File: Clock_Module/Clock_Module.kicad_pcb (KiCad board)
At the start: 2 copper layers, 160 x 100 mm, 4 parts

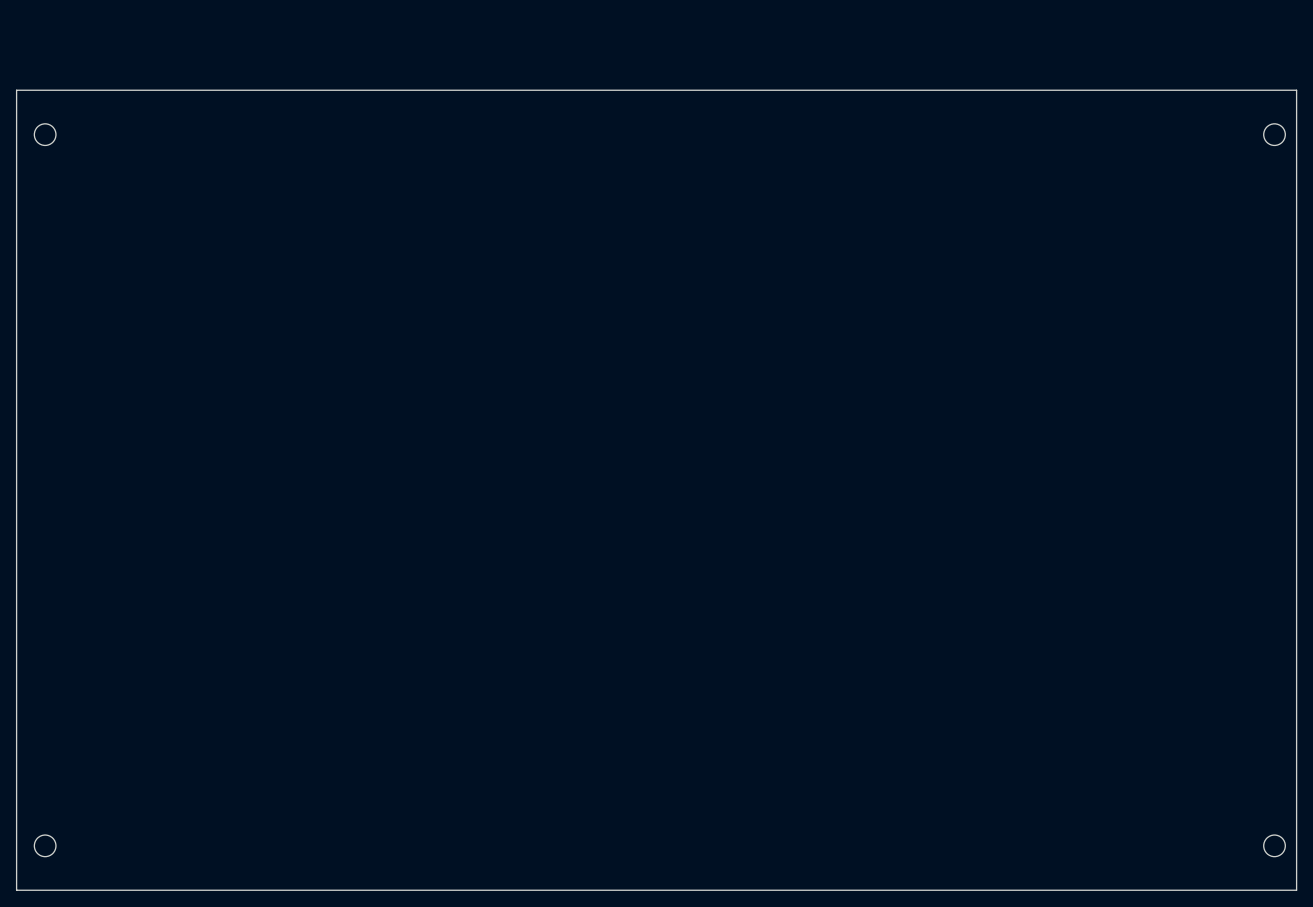
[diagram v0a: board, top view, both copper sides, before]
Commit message: Updated Schematic to PC104 standards, updated Simulation for intel-quartus, updated PCB constraints, and edited board layout
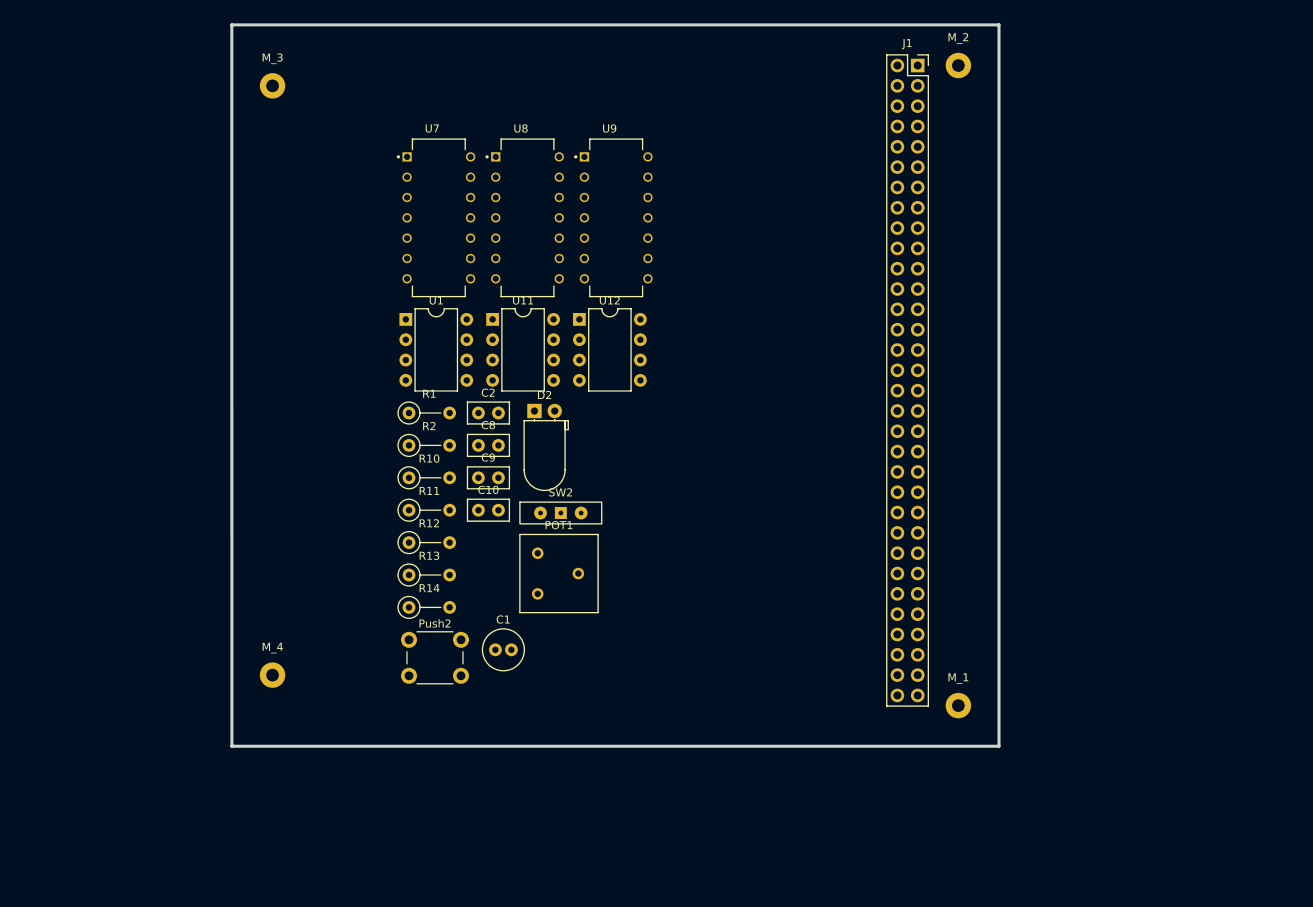
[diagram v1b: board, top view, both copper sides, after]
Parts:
- removed MH1, MH2, MH3, MH4: MountingHole_2.7mm_M2.5_DIN965, MountingHole:MountingHole_2.7mm_M2.5_DIN965
- added C1: 1µF, Capacitor_THT:C_Radial_D5.0mm_H11.0mm_P2.00mm, F.Cu at (114.8, 114.9)
- added C10: .01µF, Capacitor_THT:C_Disc_D5.0mm_W2.5mm_P2.50mm, F.Cu at (112.7, 97.5)
- added C2: .01µF, Capacitor_THT:C_Disc_D5.0mm_W2.5mm_P2.50mm, F.Cu at (112.7, 85.3)
- added C8: .01µF, Capacitor_THT:C_Disc_D5.0mm_W2.5mm_P2.50mm, F.Cu at (112.7, 89.4)
- added C9: .01µF, Capacitor_THT:C_Disc_D5.0mm_W2.5mm_P2.50mm, F.Cu at (112.7, 93.4)
- added D2: LED, LED_THT:LED_D5.0mm_Horizontal_O1.27mm_Z3.0mm, F.Cu at (119.7, 85.1)
- added J1: PC104, Connector_PinSocket_2.54mm:PinSocket_2x32_P2.54mm_Vertical, F.Cu at (167.6, 41.9)
- added M_1: MountingHole_2.5mm_Pad, MountingHole:MountingHole_2.5mm_Pad, F.Cu at (172.7, 121.9)
- added M_2: MountingHole_2.5mm_Pad, MountingHole:MountingHole_2.5mm_Pad, F.Cu at (172.7, 41.9)
- added M_3: MountingHole_2.5mm_Pad, MountingHole:MountingHole_2.5mm_Pad, F.Cu at (87.0, 44.5)
- added M_4: MountingHole_2.5mm_Pad, MountingHole:MountingHole_2.5mm_Pad, F.Cu at (87.0, 118.1)
- added POT1: 1M, Potentiometer_THT:Potentiometer_Bourns_3386F_Vertical, F.Cu at (120.1, 108.0)
- added Push2: SW_Push, Button_Switch_THT:SW_PUSH_6mm_H4.3mm, F.Cu at (104.0, 113.7)
- added R1: 1K, Resistor_THT:R_Axial_DIN0207_L6.3mm_D2.5mm_P5.08mm_Vertical, F.Cu at (104.0, 85.3)
- added R10: 1K, Resistor_THT:R_Axial_DIN0207_L6.3mm_D2.5mm_P5.08mm_Vertical, F.Cu at (104.0, 93.4)
- added R11: 1K, Resistor_THT:R_Axial_DIN0207_L6.3mm_D2.5mm_P5.08mm_Vertical, F.Cu at (104.0, 97.5)
- added R12: 1K, Resistor_THT:R_Axial_DIN0207_L6.3mm_D2.5mm_P5.08mm_Vertical, F.Cu at (104.0, 101.5)
- added R13: 1M, Resistor_THT:R_Axial_DIN0207_L6.3mm_D2.5mm_P5.08mm_Vertical, F.Cu at (104.0, 105.6)
- added R14: 1K, Resistor_THT:R_Axial_DIN0207_L6.3mm_D2.5mm_P5.08mm_Vertical, F.Cu at (104.0, 109.6)
- added R2: 1K, Resistor_THT:R_Axial_DIN0207_L6.3mm_D2.5mm_P5.08mm_Vertical, F.Cu at (104.0, 89.4)
- added SW2: SW_Wuerth_450301014042, MyFootPrints:SW_Slide-Jameco-SS-12E17-G020, F.Cu at (123.0, 97.8)
- added U1: LM555xN, Package_DIP:DIP-8_W7.62mm, F.Cu at (103.7, 73.6)
- added U11: LM555xN, Package_DIP:DIP-8_W7.62mm, F.Cu at (114.5, 73.6)
- added U12: LM555xN, Package_DIP:DIP-8_W7.62mm, F.Cu at (125.3, 73.6)
- added U7: 74LS08, MyFootPrints:SN74LS08N, F.Cu at (107.8, 61.0)
- added U8: 74LS32, MyFootPrints:SN74LS32N, F.Cu at (118.9, 61.0)
- added U9: 74LS04, MyFootPrints:SN74LS04N, F.Cu at (129.9, 61.0)
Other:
- board size 160 x 100 mm -> 95.9 x 90.2 mm
- board text removed: "Mounting holes are optional Keepout areas are for for guide rails"

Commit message: partially complete pcb and updated schematic with bypass capacitors
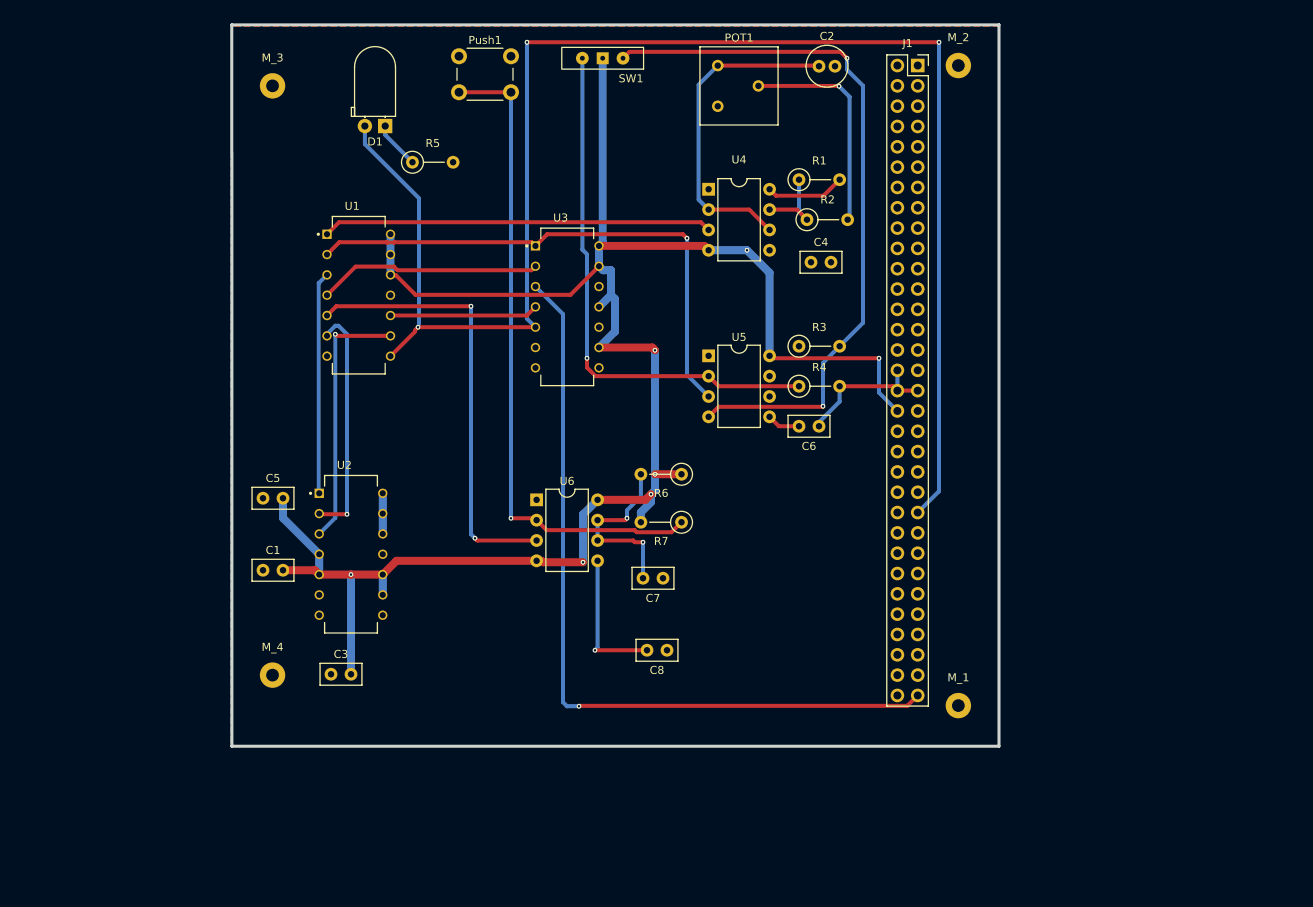
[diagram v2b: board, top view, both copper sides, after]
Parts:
- removed C10, C9: .01µF, Capacitor_THT:C_Disc_D5.0mm_W2.5mm_P2.50mm
- removed D2: LED, LED_THT:LED_D5.0mm_Horizontal_O1.27mm_Z3.0mm
- removed Push2: SW_Push, Button_Switch_THT:SW_PUSH_6mm_H4.3mm
- removed R10, R11, R12, R14: 1K, Resistor_THT:R_Axial_DIN0207_L6.3mm_D2.5mm_P5.08mm_Vertical
- removed R13: 1M, Resistor_THT:R_Axial_DIN0207_L6.3mm_D2.5mm_P5.08mm_Vertical
- removed SW2: SW_Wuerth_450301014042, MyFootPrints:SW_Slide-Jameco-SS-12E17-G020
- removed U11, U12: LM555xN, Package_DIP:DIP-8_W7.62mm
- removed U7: 74LS08, MyFootPrints:SN74LS08N
- removed U8: 74LS32, MyFootPrints:SN74LS32N
- removed U9: 74LS04, MyFootPrints:SN74LS04N
- added C3: .01µF, Capacitor_THT:C_Disc_D5.0mm_W2.5mm_P2.50mm, F.Cu at (94.3, 118.0)
- added C4: .01µF, Capacitor_THT:C_Disc_D5.0mm_W2.5mm_P2.50mm, F.Cu at (154.3, 66.5)
- added C5: .01µF, Capacitor_THT:C_Disc_D5.0mm_W2.5mm_P2.50mm, F.Cu at (85.8, 96.0)
- added C6: .01µF, Capacitor_THT:C_Disc_D5.0mm_W2.5mm_P2.50mm, F.Cu at (155.3, 87.0)
- added C7: .01µF, Capacitor_THT:C_Disc_D5.0mm_W2.5mm_P2.50mm, F.Cu at (135.8, 106.0)
- added D1: LED, LED_THT:LED_D5.0mm_Horizontal_O1.27mm_Z3.0mm, F.Cu at (101.1, 49.5)
- added Push1: SW_Push, Button_Switch_THT:SW_PUSH_6mm_H4.3mm, F.Cu at (110.3, 40.8)
- added R3: 1K, Resistor_THT:R_Axial_DIN0207_L6.3mm_D2.5mm_P5.08mm_Vertical, F.Cu at (152.8, 77.0)
- added R4: 1K, Resistor_THT:R_Axial_DIN0207_L6.3mm_D2.5mm_P5.08mm_Vertical, F.Cu at (152.8, 82.0)
- added R5: 1K, Resistor_THT:R_Axial_DIN0207_L6.3mm_D2.5mm_P5.08mm_Vertical, F.Cu at (104.5, 54.0)
- added R6: 1M, Resistor_THT:R_Axial_DIN0207_L6.3mm_D2.5mm_P5.08mm_Vertical, F.Cu at (138.1, 93.0)
- added R7: 1K, Resistor_THT:R_Axial_DIN0207_L6.3mm_D2.5mm_P5.08mm_Vertical, F.Cu at (138.1, 99.0)
- added SW1: Switch, MyFootPrints:SW_Slide-Jameco-SS-12E17-G020, F.Cu at (128.3, 41.0)
- added U2: 74LS32, MyFootPrints:SN74LS32N, F.Cu at (96.8, 103.0)
- added U3: 74LS04, MyFootPrints:SN74LS04N, F.Cu at (123.8, 72.1)
- added U4: LM555xN, Package_DIP:DIP-8_W7.62mm, F.Cu at (141.5, 57.4)
- added U5: LM555xN, Package_DIP:DIP-8_W7.62mm, F.Cu at (141.5, 78.2)
- added U6: LM555xN, Package_DIP:DIP-8_W7.62mm, F.Cu at (120.0, 96.2)
- C1: value 1µF -> .01µF; footprint Capacitor_THT:C_Radial_D5.0mm_H11.0mm_P2.00mm -> Capacitor_THT:C_Disc_D5.0mm_W2.5mm_P2.50mm
- C2: value .01µF -> 1µF; footprint Capacitor_THT:C_Disc_D5.0mm_W2.5mm_P2.50mm -> Capacitor_THT:C_Radial_D5.0mm_H11.0mm_P2.00mm
- U1: value LM555xN -> 74LS08; footprint Package_DIP:DIP-8_W7.62mm -> MyFootPrints:SN74LS08N
- moved POT1 65.0 mm to (142.6, 47.0)
- moved C2 60.8 mm to (155.3, 42.0)
- moved R2 57.2 mm to (153.8, 61.2)
- moved R1 56.8 mm to (152.8, 56.2)
- moved C8 34.8 mm to (136.3, 115.0), turned to 180 degrees
- moved C1 30.7 mm to (85.8, 105.0)
- moved U1 6.61 mm to (97.8, 70.6)
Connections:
- C1 pad 1: Net-(U1-THR) -> GND
- C1 pad 2: GND -> 5V
- C2 pad 1: GND -> Net-(U4-THR)
- POT1 pad 3: Net-(U1-THR) -> Net-(U4-THR)
- R1 pad 1: Net-(U1-DIS) -> Net-(U4-DIS)
- R2 pad 1: Net-(U1-DIS) -> Net-(U4-DIS)
- U1 pad 1: GND -> /astable_out
- U1 pad 2: Net-(U1-THR) -> /bistable_out
- U1 pad 3: /astable_out -> Net-(U1-Pad3)
- U1 pad 4: 5V -> Net-(U1-Pad4)
- U1 pad 5: GND -> /monostable_out
- U1 pad 6: Net-(U1-THR) -> Net-(U1-Pad6)
- U1 pad 7: Net-(U1-DIS) -> GND
- U1 pad 8: 5V -> /CLK
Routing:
- net 5V: track 0.00 -> 256.9 mm, vias 0 -> 7
- net /CLK: track 0.00 -> 195.2 mm, vias 0 -> 3
- net /halt: track 0.00 -> 98.5 mm, vias 0 -> 1
- net Net-(SW1-C): track 0.00 -> 89.9 mm, vias 0 -> 2
- net Net-(U6-TR): track 0.00 -> 82.3 mm, vias 0 -> 1
- net /bistable_out: track 0.00 -> 67.6 mm, vias 0 -> 1
- net Net-(SW1-A): track 0.00 -> 66.4 mm, vias 0 -> 1
- net /monostable_out: track 0.00 -> 55.5 mm, vias 0 -> 2
- net /astable_out: track 0.00 -> 48.7 mm
- net Net-(U4-THR): track 0.00 -> 40.9 mm
- net Net-(U1-Pad9): track 0.00 -> 32.8 mm, vias 0 -> 1
- net Net-(U1-Pad6): track 0.00 -> 29.6 mm, vias 0 -> 1
- net Net-(U1-Pad4): track 0.00 -> 27.9 mm
- net Net-(U1-Pad3): track 0.00 -> 27.8 mm
- net Net-(POT1-Pad2): track 0.00 -> 27.4 mm, vias 0 -> 1
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- added copper zone on B.Cu, net GND
- added copper zone on F.Cu, net GND

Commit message: Routed PCB
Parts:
- added ?: , PCB_Art:GrayFox.F.Cu, F.Cu at (150.3, 107.0)
- added ?: , PCB_Art:GrayFox.F.SilkS, F.Cu at (150.3, 107.0)
- added ?: , PCB_Art:GrayFox.F.Mask, F.Cu at (150.3, 107.0)
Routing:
- net /CLK: track 195.2 -> 118.1 mm, vias 3 -> 4
- net 5V: track 256.9 -> 310.9 mm
- net /astable_out: track 48.7 -> 50.4 mm
- net Net-(U1-Pad6): track 29.6 -> 31.2 mm
- net Net-(U1-Pad9): track 32.8 -> 31.9 mm
- net GND: track 18.6 -> 19.1 mm

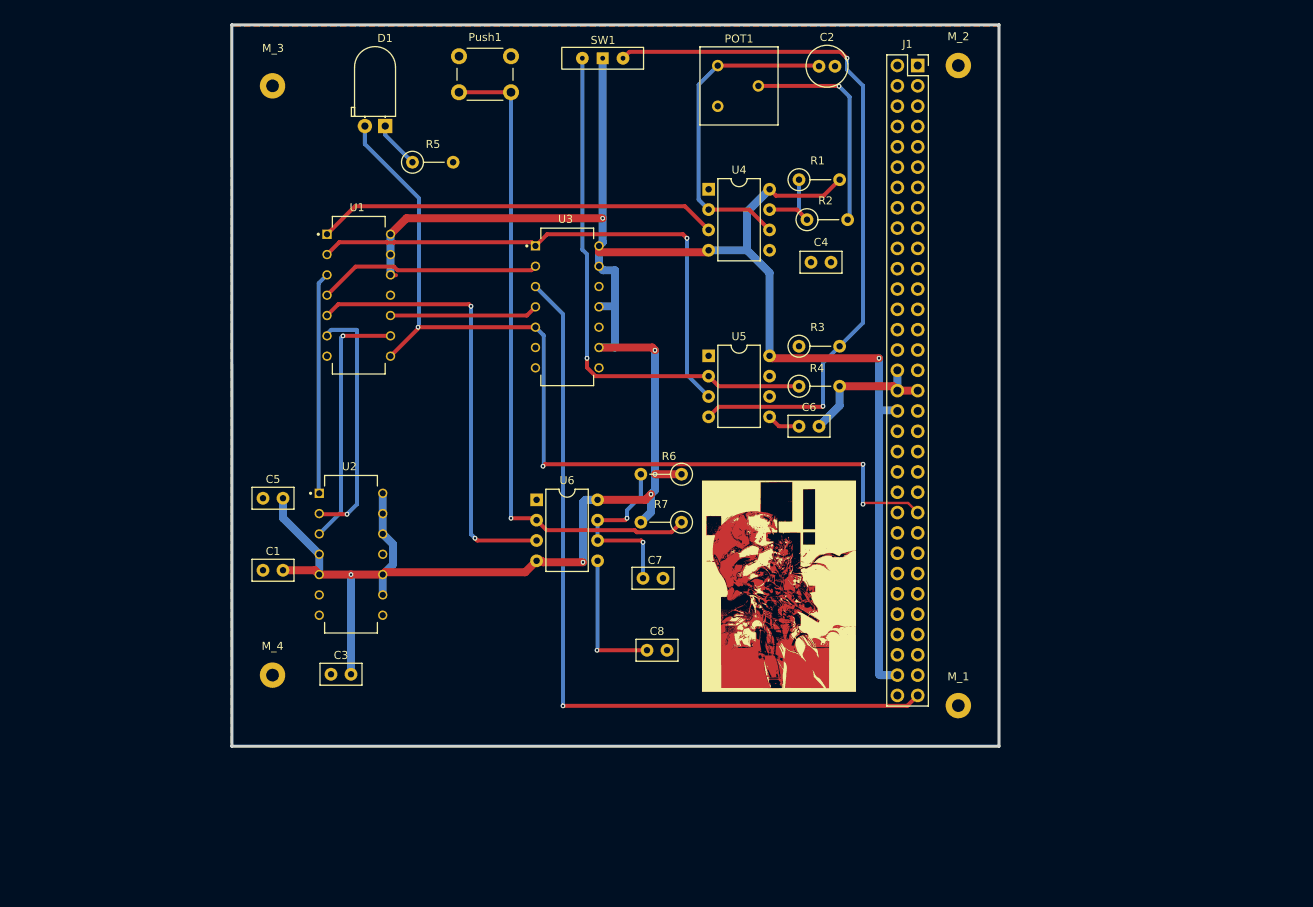
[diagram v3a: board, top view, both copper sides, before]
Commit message: completed clock module
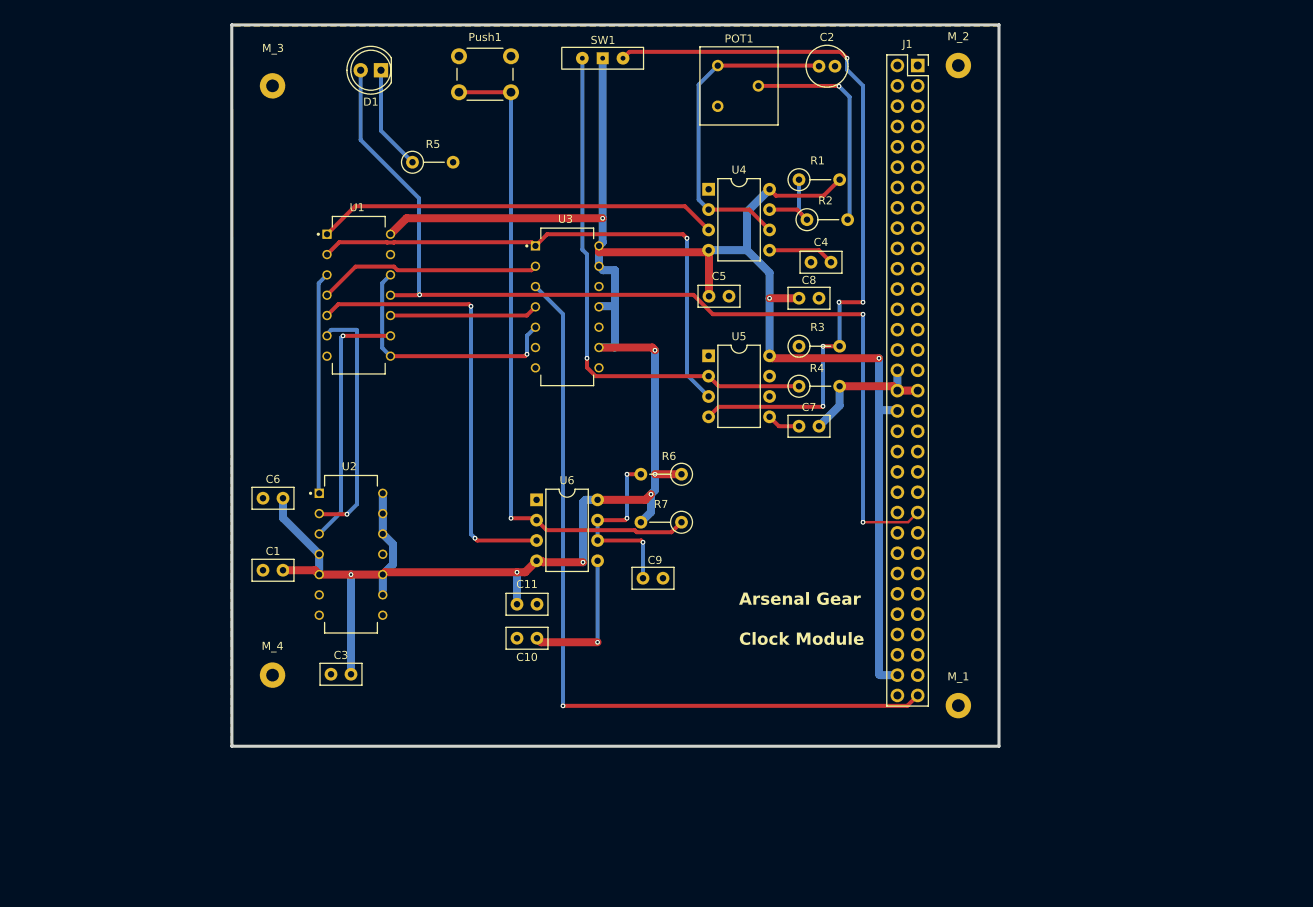
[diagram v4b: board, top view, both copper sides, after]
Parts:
- removed ?: , PCB_Art:GrayFox.F.Cu
- removed ?: , PCB_Art:GrayFox.F.SilkS
- removed ?: , PCB_Art:GrayFox.F.Mask
- added C11: 47uF, Capacitor_THT:C_Disc_D5.0mm_W2.5mm_P2.50mm, F.Cu at (117.5, 109.2)
- added C5: 47µF, Capacitor_THT:C_Disc_D5.0mm_W2.5mm_P2.50mm, F.Cu at (141.6, 70.8)
- added C8: 47uF, Capacitor_THT:C_Disc_D5.0mm_W2.5mm_P2.50mm, F.Cu at (155.3, 71.0)
- D1: footprint LED_THT:LED_D5.0mm_Horizontal_O1.27mm_Z3.0mm -> LED_THT:LED_D5.0mm
- moved C10 18.8 mm to (117.5, 113.5), turned to 0 degrees
- moved D1 6.99 mm to (100.5, 42.5)
- renumbered C8 to C10, C5 to C6, C6 to C7, C7 to C9
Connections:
- C4 pad 2: GND -> Net-(U4-CV)
- U1 pad 11: unconnected-(U1-Pad11) -> /CLK
- U1 pad 12: 5V -> Net-(U1-Pad12)
- U1 pad 13: 5V -> GND
- U1 pad 8: /CLK -> Net-(U1-Pad12)
- U3 pad 5: /CLK -> Net-(U1-Pad12)
- U4 pad 5: GND -> Net-(U4-CV)
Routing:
- net Net-(U1-Pad12): track 0.00 -> 32.0 mm, vias 0 -> 1
- net Net-(U4-CV): track 0.00 -> 8.30 mm
- net 5V: track 310.9 -> 318.6 mm, vias 7 -> 9
- net Net-(D1-K): track 5.94 -> 13.1 mm
- net /CLK: track 118.1 -> 124.6 mm, vias 4 -> 3
- net Net-(SW1-C): track 89.9 -> 93.1 mm, vias 2 -> 5
- net Net-(U6-DIS): track 22.8 -> 23.8 mm, vias 2 -> 3
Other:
- board text added: "Arsenal Gear"
- board text added: "Clock Module"
